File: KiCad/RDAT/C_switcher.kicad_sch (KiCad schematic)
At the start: 31 parts, among them J3 USB_C_Receptacle, U6 PTPS25751DREFR

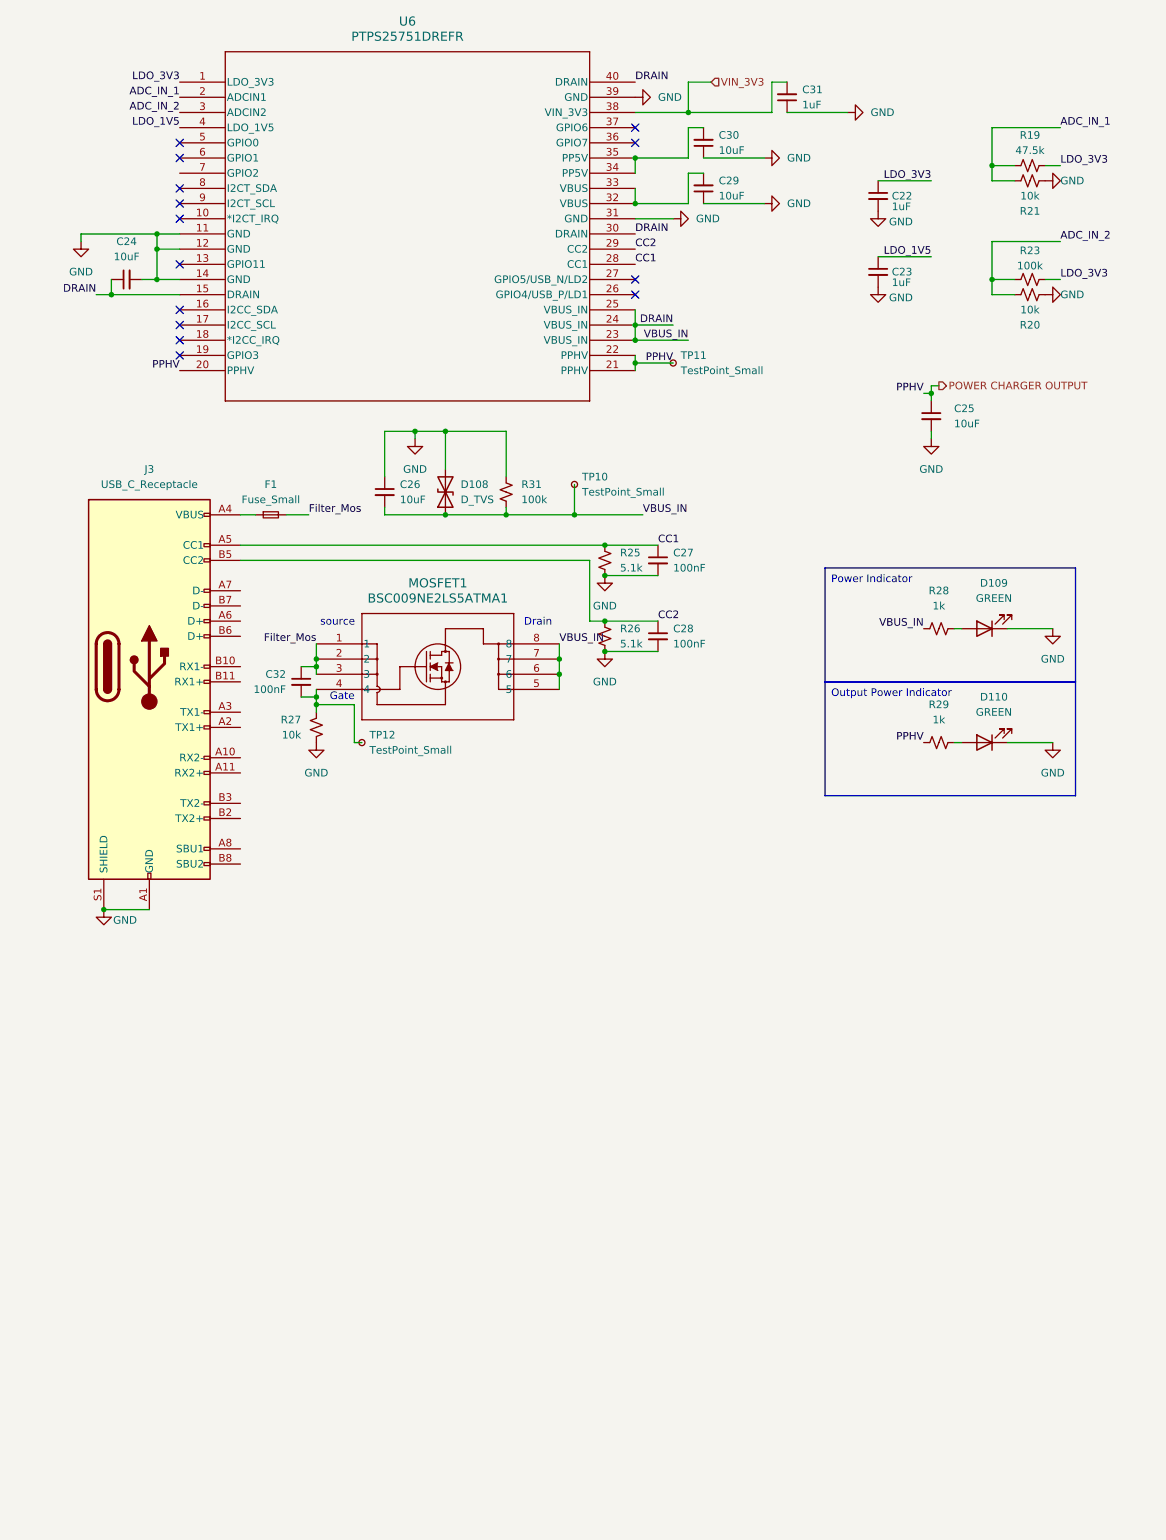
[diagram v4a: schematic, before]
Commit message: Add new notes; update component references in schematics and footprints, and complete charging design
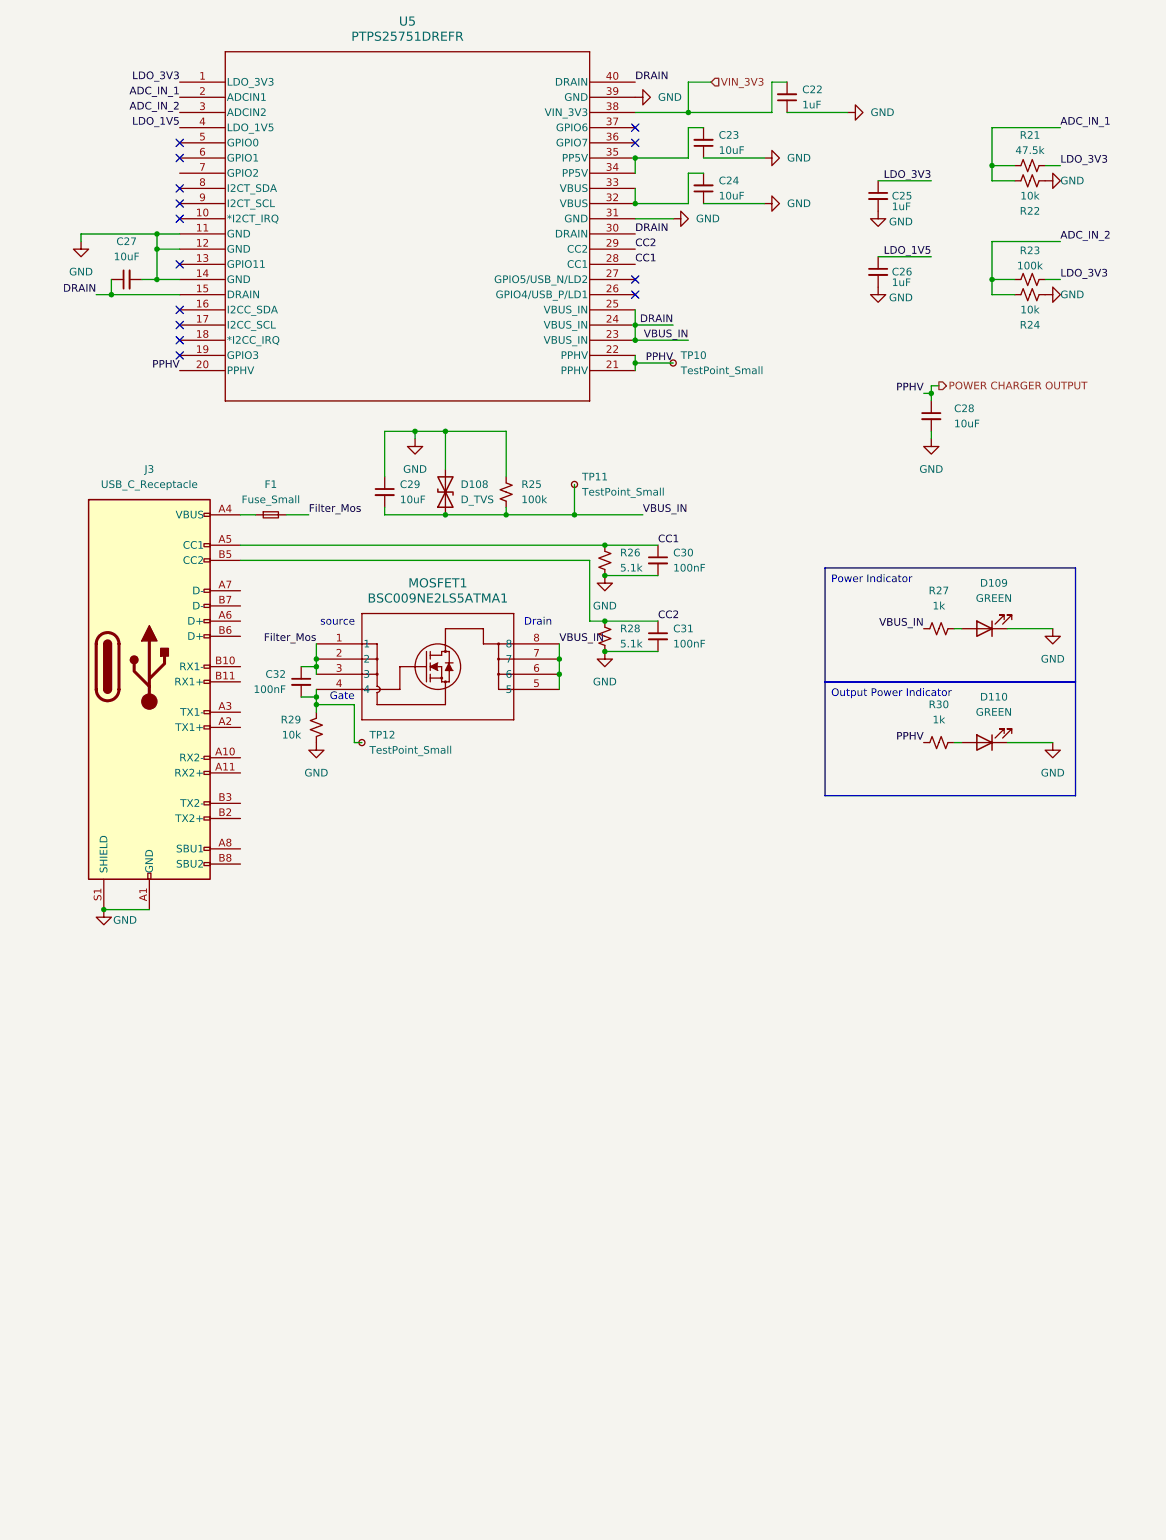
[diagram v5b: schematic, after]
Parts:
- renumbered C31 to C22, C30 to C23, C29 to C24, C22 to C25, C23 to C26, C24 to C27, C25 to C28, C26 to C29, C27 to C30, C28 to C31, R19 to R21, R21 to R22, R20 to R24, R31 to R25, R25 to R26, R28 to R27, R26 to R28, R27 to R29, R29 to R30, TP11 to TP10, TP10 to TP11, U6 to U5

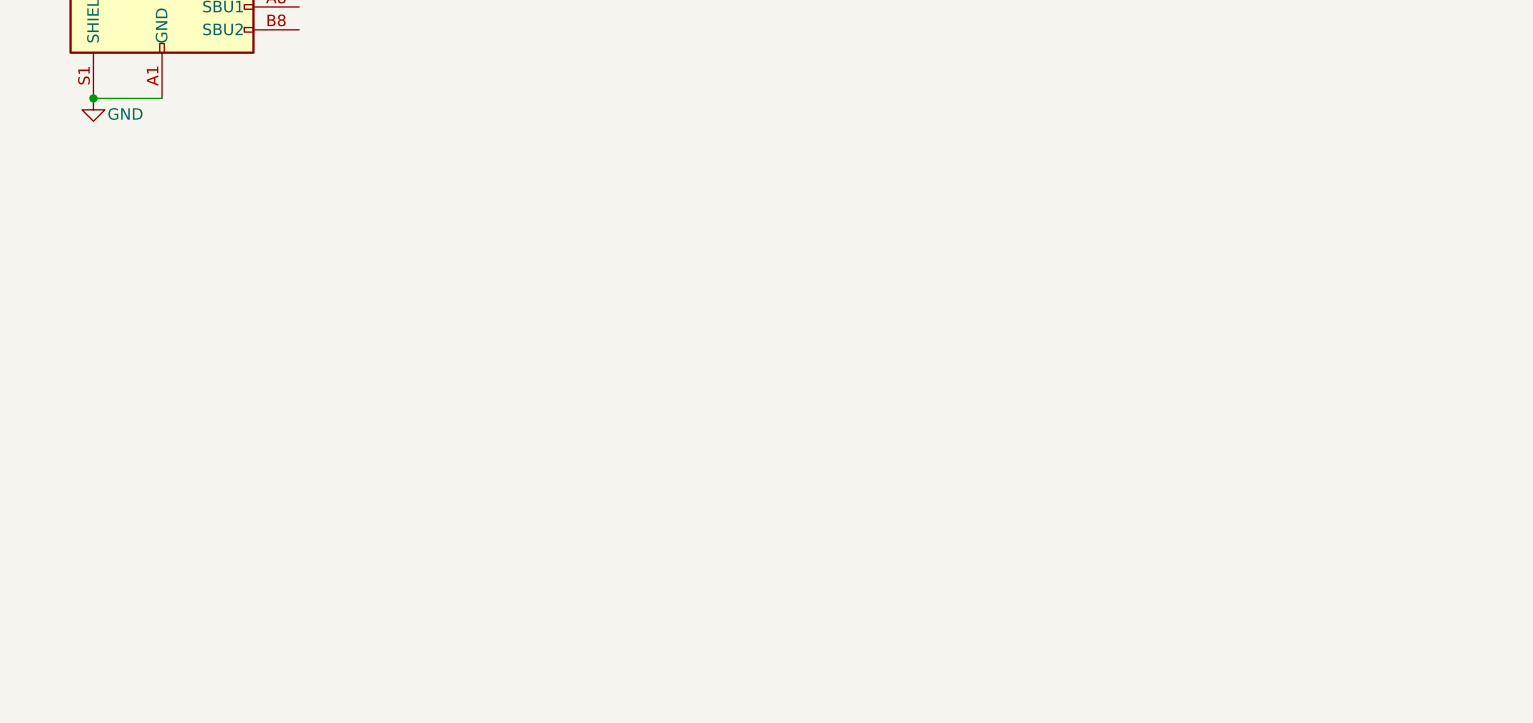
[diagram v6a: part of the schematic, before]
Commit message: Added example and updated power path
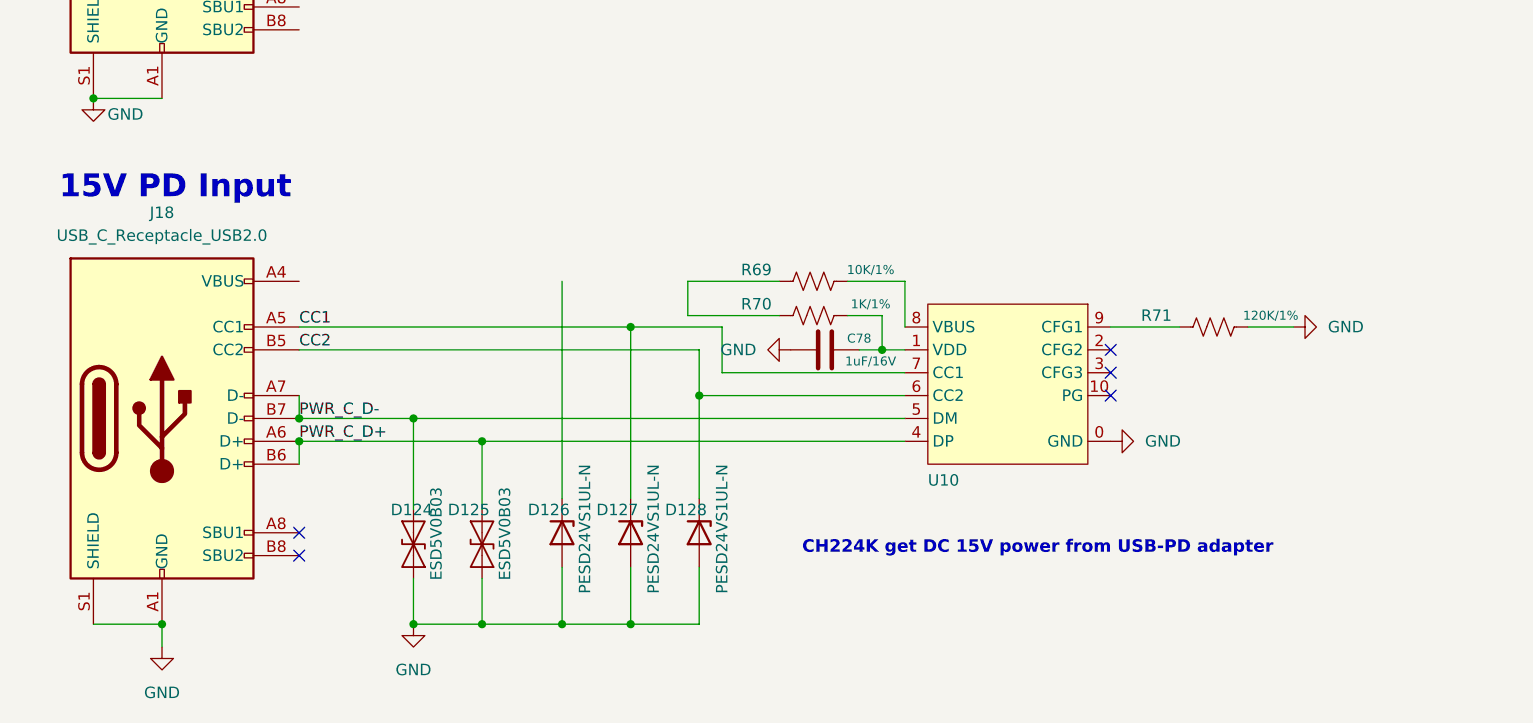
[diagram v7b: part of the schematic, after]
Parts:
- added C78: 1uF/16V, A_HDJ_Library:C_0402_1005Metric, symbol Device:C
- added D124, D125: ESD5V0B03, A_HDJ_Library:D_0402_1005Metric, symbol Diode:ESD9B5.0ST5G
- added D126, D127, D128: PESD24VS1UL-N, A_HDJ_Library:D_0402_1005Metric, symbol Device:D_Zener
- added J18: USB_C_Receptacle_USB2.0, A_HDJ_Library:USB_C_Receptacle_G-Switch_GT-USB-7010ASV, symbol Connector:USB_C_Receptacle_USB2.0_16P
- added R69: 10K/1%, A_HDJ_Library:R_0402_1005Metric, symbol Device:R_US
- added R70: 1K/1%, A_HDJ_Library:R_0402_1005Metric, symbol Device:R_US
- added R71: 120K/1%, A_HDJ_Library:R_0402_1005Metric, symbol Device:R_US
- added U10: CH224Q, A_HDJ_Library:ESSOP-10-1EP_3.9x5mm_P1.0mm_EP3.2x2.3, symbol A_HDJ_Library:CH224K
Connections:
- net CC1: now also D127.1 (K), J18.A5 (CC1), U10.7 (CC1)
- net CC2: now also D128.1 (K), J18.B5 (CC2), U10.6 (CC2)
- net GND: now also C78.2, D124.1 (A1), D125.1 (A1), D126.2 (A), D127.2 (A), D128.2 (A), J18.A1 (GND), J18.A12 (GND), J18.B1 (GND), J18.B12 (GND), J18.S1 (SHIELD), R71.2, U10.0 (GND)
- new net: J18.A4 (VBUS), J18.A9 (VBUS), J18.B4 (VBUS), J18.B9 (VBUS)
- new net: C78.1, R70.2, U10.1 (VDD)
- new net: R69.2, U10.8 (VBUS)
- new net: R71.1, U10.9 (CFG1)
- new net: R69.1, R70.1
- new net PWR_C_D+: D125.2 (A2), J18.A6 (D+), J18.B6 (D+), U10.4 (DP)
- new net PWR_C_D-: D124.2 (A2), J18.A7 (D-), J18.B7 (D-), U10.5 (DM)
- no-connect marks 14 -> 19
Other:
- note added: "15V PD Input"
- note added: "CH224K get DC 15V power from USB-PD adapter"

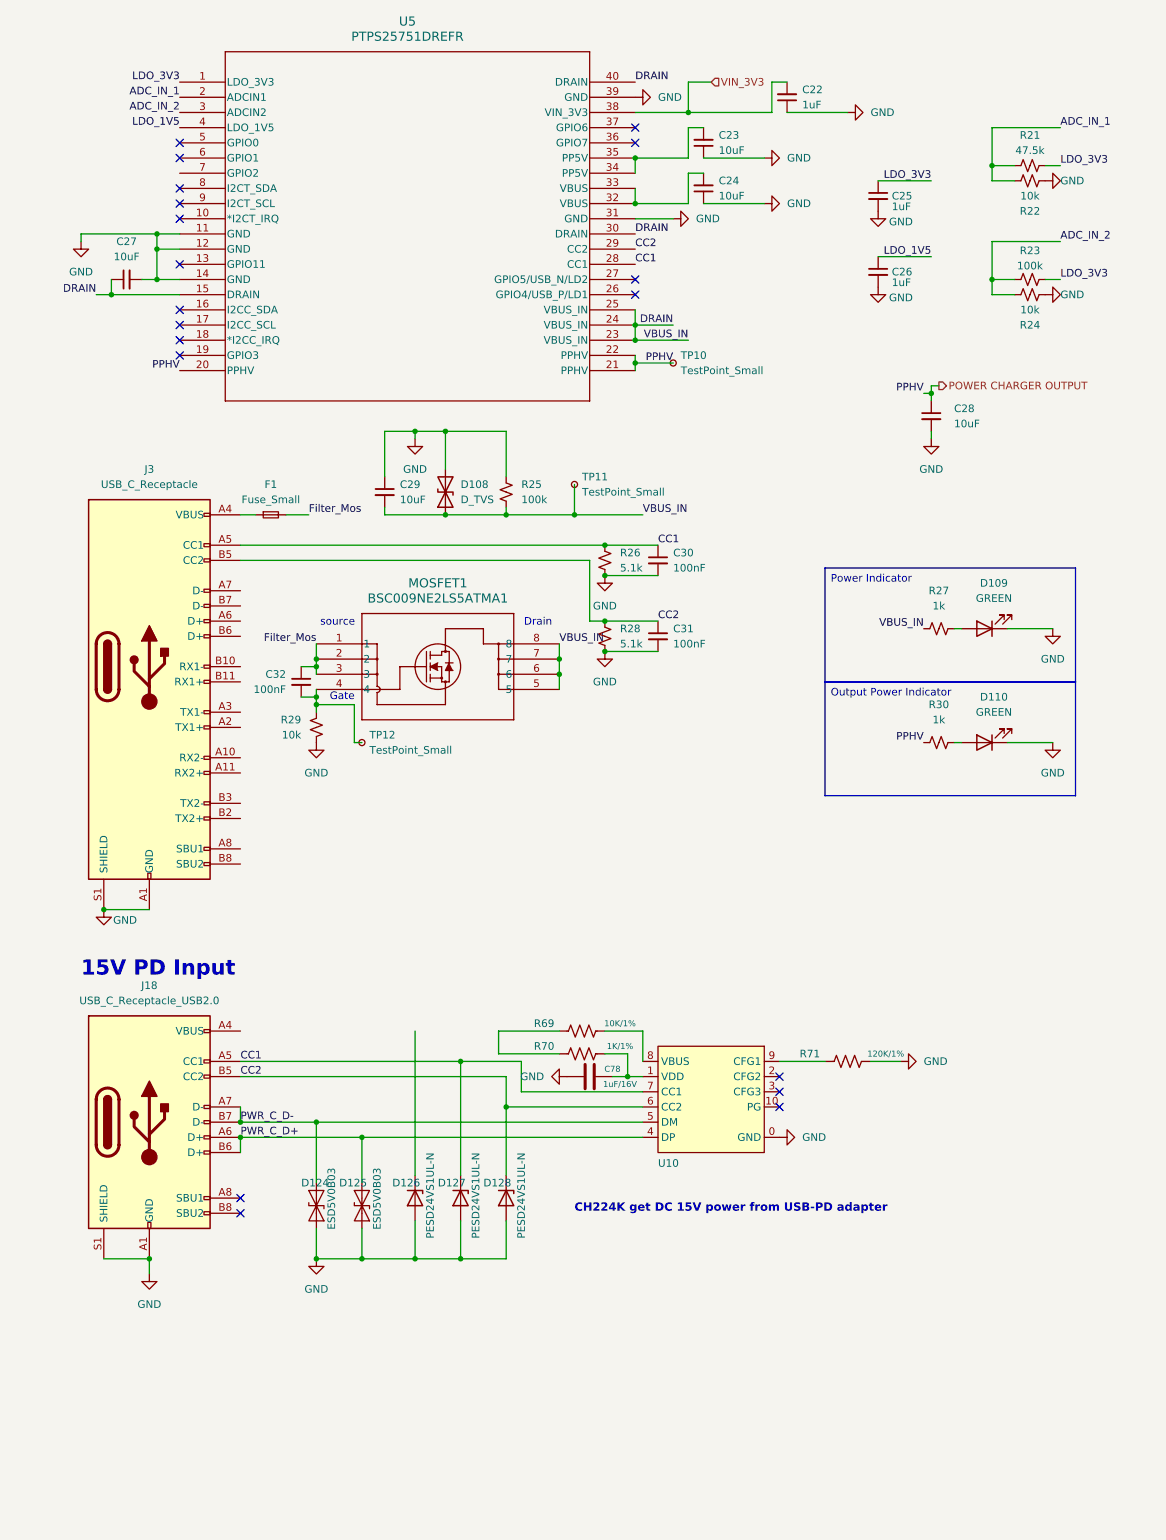
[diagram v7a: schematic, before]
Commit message: Modified Power Stages
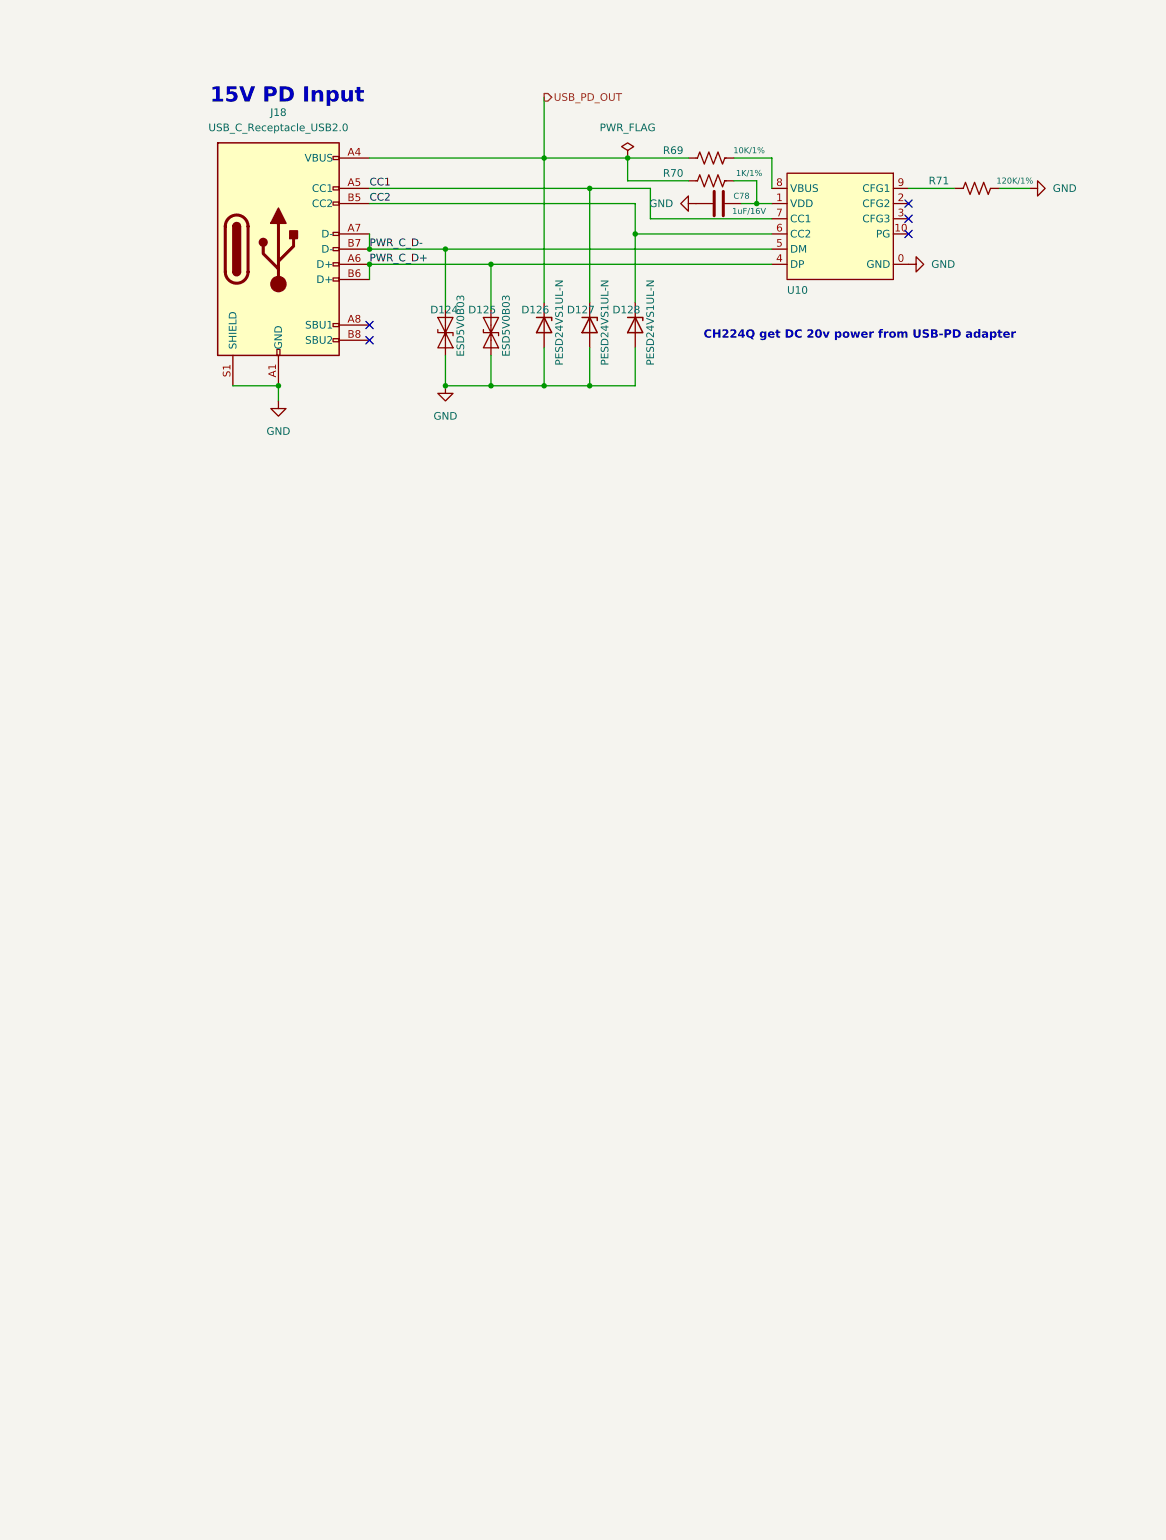
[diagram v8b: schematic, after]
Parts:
- removed C22, C25, C26: 1uF, symbol Device:C_Small
- removed C23, C24, C27, C28, C29: 10uF, symbol Device:C_Small
- removed C30, C31, C32: 100nF, symbol Device:C_Small
- removed D108: D_TVS, symbol Device:D_TVS
- removed D109, D110: GREEN, symbol Device:LED
- removed F1: Fuse_Small, symbol Device:Fuse_Small
- removed J3: USB_C_Receptacle, symbol Connector:USB_C_Receptacle
- removed MOSFET1: BSC009NE2LS5ATMA1, PG-TDSON-8-1_INF, symbol BSC009NE2LS5ATMA1:BSC009NE2LS5ATMA1
- removed R21: 47.5k, symbol Device:R_Small_US
- removed R22, R24, R29: 10k, symbol Device:R_Small_US
- removed R23, R25: 100k, symbol Device:R_Small_US
- removed R26, R28: 5.1k, symbol Device:R_Small_US
- removed R27, R30: 1k, symbol Device:R_Small_US
- removed TP10, TP11, TP12: TestPoint_Small, symbol Connector:TestPoint_Small
- removed U5: PTPS25751DREFR, WQFN38_REF_TEX, symbol TPS25751:PTPS25751DREFR
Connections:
- net USB_PD_OUT: now reaches J18.A4 (VBUS), J18.A9 (VBUS), J18.B4 (VBUS), J18.B9 (VBUS)
- net USB_PD_OUT: now also D126.1 (K), R69.1, R70.1
- no-connect marks 19 -> 5
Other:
- note added: "CH224Q get DC 20v power from USB-PD adapter"
- note removed: "CH224K get DC 15V power from USB-PD adapter"
- note removed: "Drain"
- note removed: "Gate"
- note removed: "source"
- moved on the sheet: C78, D124, D125, D126, D127, D128, J18, R69, R70, R71, U10
